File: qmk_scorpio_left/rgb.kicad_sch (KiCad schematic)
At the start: 64 parts

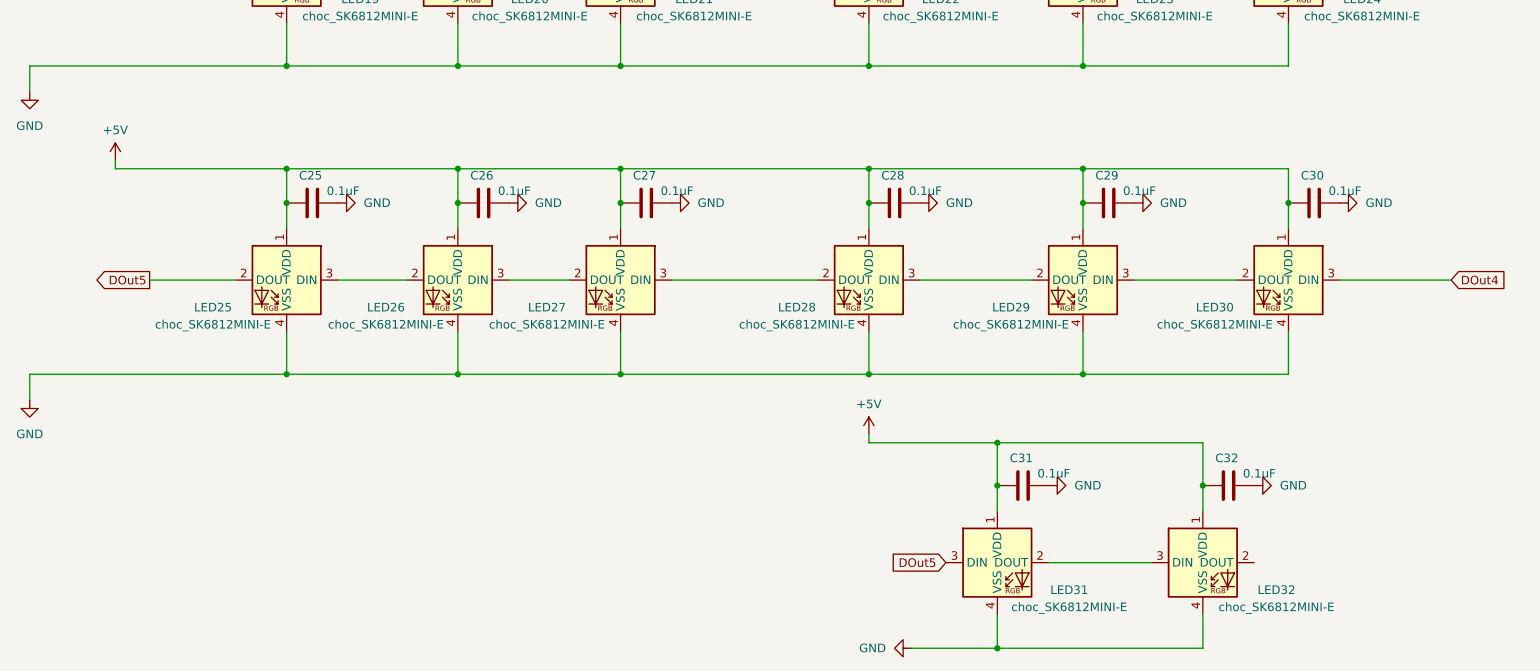
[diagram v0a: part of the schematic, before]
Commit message: pin corrections and updated rgb
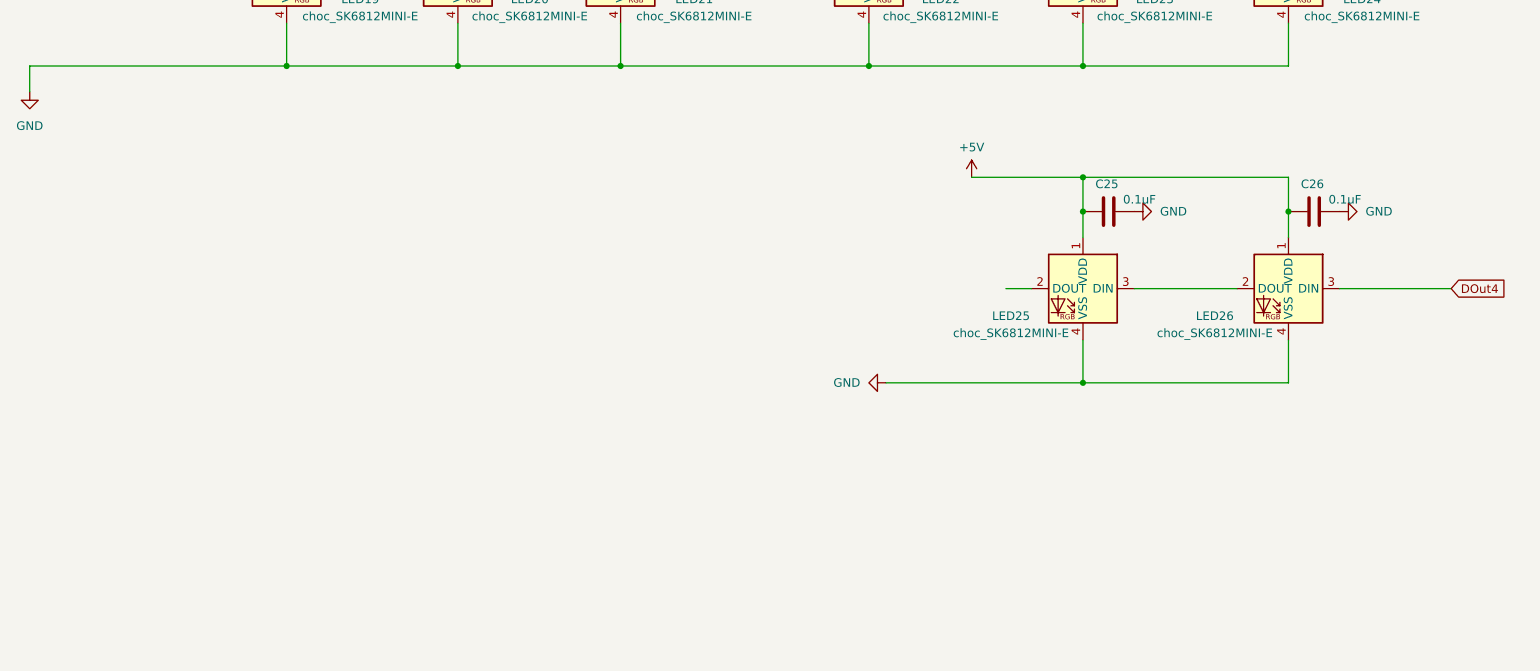
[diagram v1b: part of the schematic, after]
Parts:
- removed C25, C26, C27, C28, C31, C32: 0.1uF, Capacitor_SMD:C_0402_1005Metric, symbol Device:C
- removed LED25, LED26, LED27, LED28, LED31, LED32: choc_SK6812MINI-E, PCM_marbastlib-choc:LED_choc_6028R, symbol PCM_marbastlib-choc:choc_SK6812MINI-E
- renumbered C29 to C25, C30 to C26, LED29 to LED25, LED30 to LED26
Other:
- moved on the sheet: C25, C26, LED25, LED26

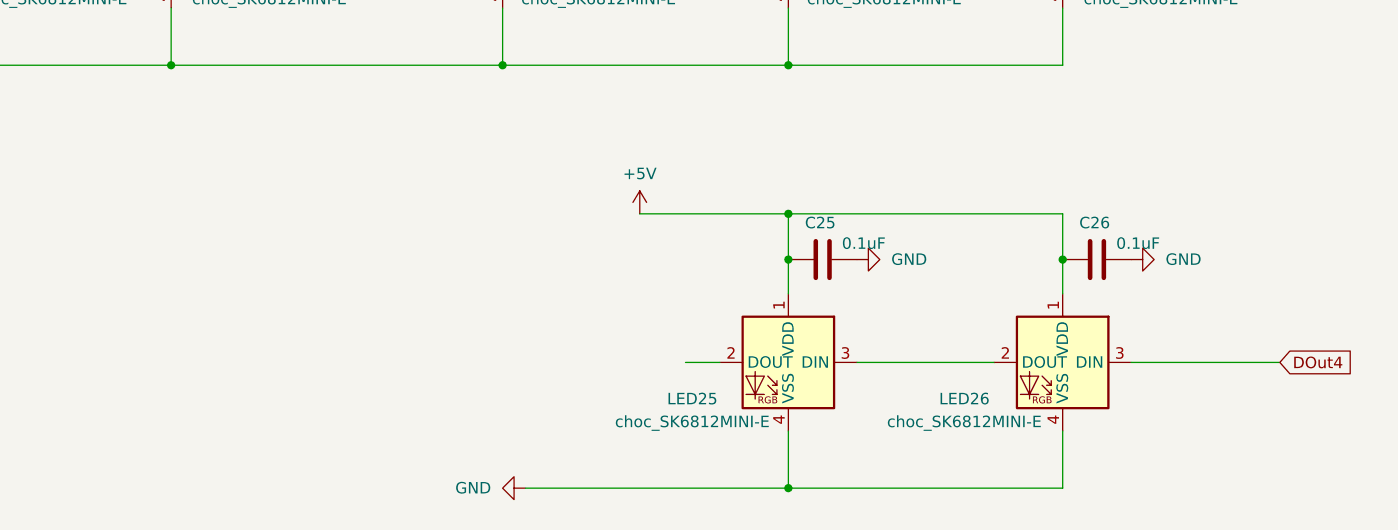
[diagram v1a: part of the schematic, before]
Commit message: placed all components on board
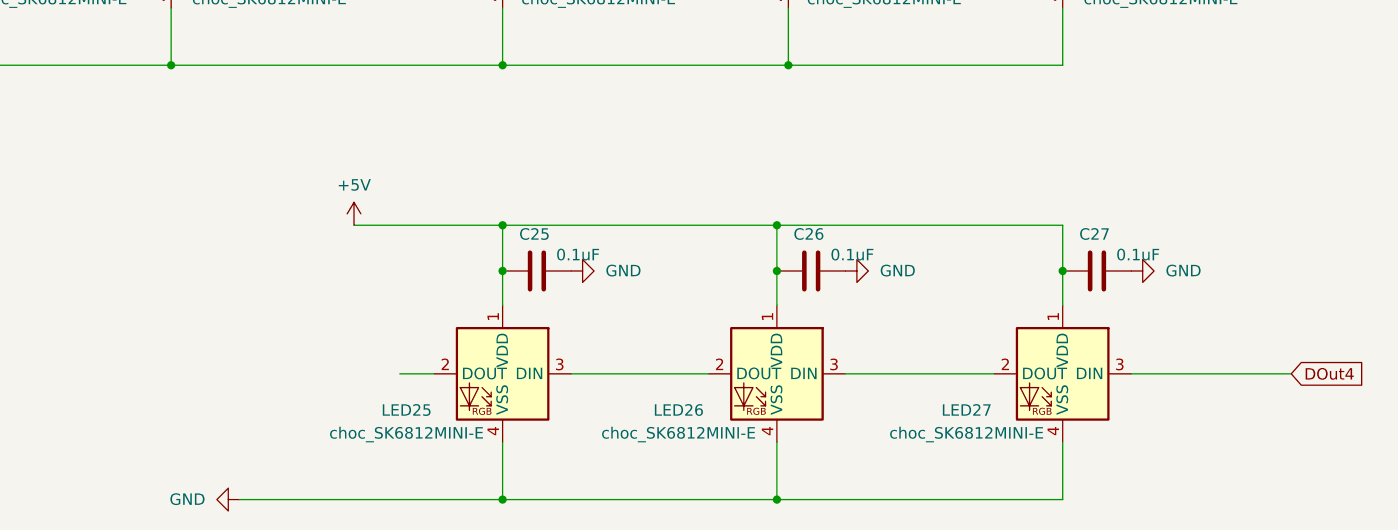
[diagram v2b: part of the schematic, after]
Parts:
- added C27: 0.1uF, Capacitor_SMD:C_0402_1005Metric, symbol Device:C
- added LED27: choc_SK6812MINI-E, PCM_marbastlib-choc:LED_choc_6028R, symbol PCM_marbastlib-choc:choc_SK6812MINI-E
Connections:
- net +5V: now also C27.1, LED27.1 (VDD)
- net DOut4: now also LED27.3 (DIN); no longer LED26.3 (DIN)
- net GND: now also C27.2, LED27.4 (VSS)
- new net: LED26.3 (DIN), LED27.2 (DOUT)
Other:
- moved on the sheet: C25, C26, LED25, LED26
